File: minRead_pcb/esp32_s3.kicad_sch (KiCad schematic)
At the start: 12 parts, among them SW12 SW_Push, SW6 SW_Push, U4 ESP32-S3-WROOM-1

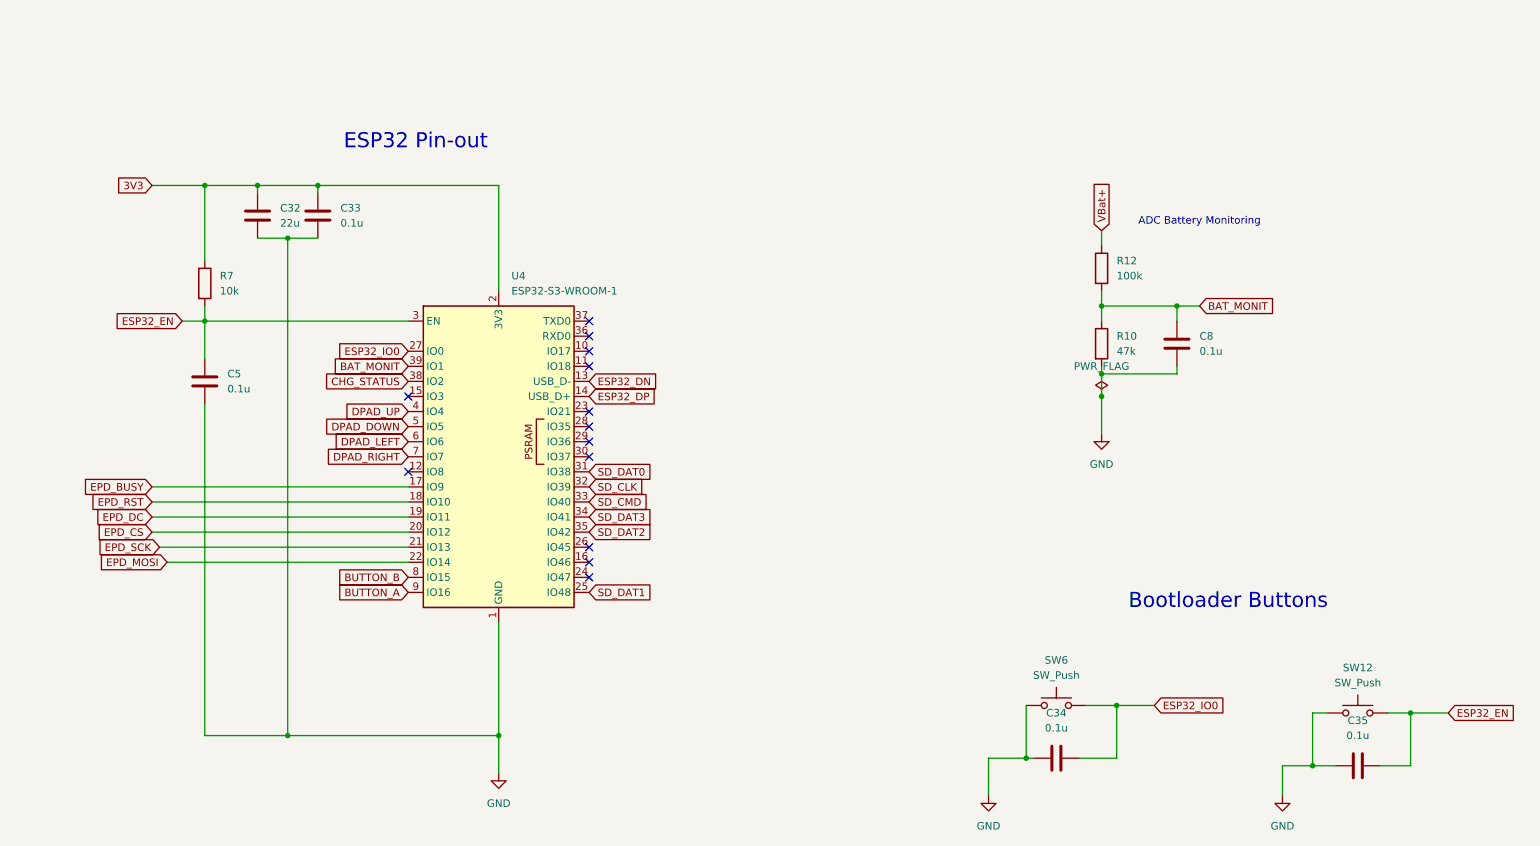
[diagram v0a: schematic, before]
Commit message: - schematic updates: - usb500 mode enabled on bq - charge limit set to 100mA 8.9kohm (safe for small batteries) - series resistors on sd card and epd lines - esd arrays for usb-c and sd-card - increased output cap for ldo from 4.7u to 22u - added pgood to gpio - confirmed reverse polarity stuff - cap to ground instead of series for sd card vdd - fixed cap values on epd
new layout:
- adjusted board size
- very compact
- need to fill ground planes and check drc errors (a lot because of solder mask)
- need to adjust jst footprint in case there's a better choice
- review review review
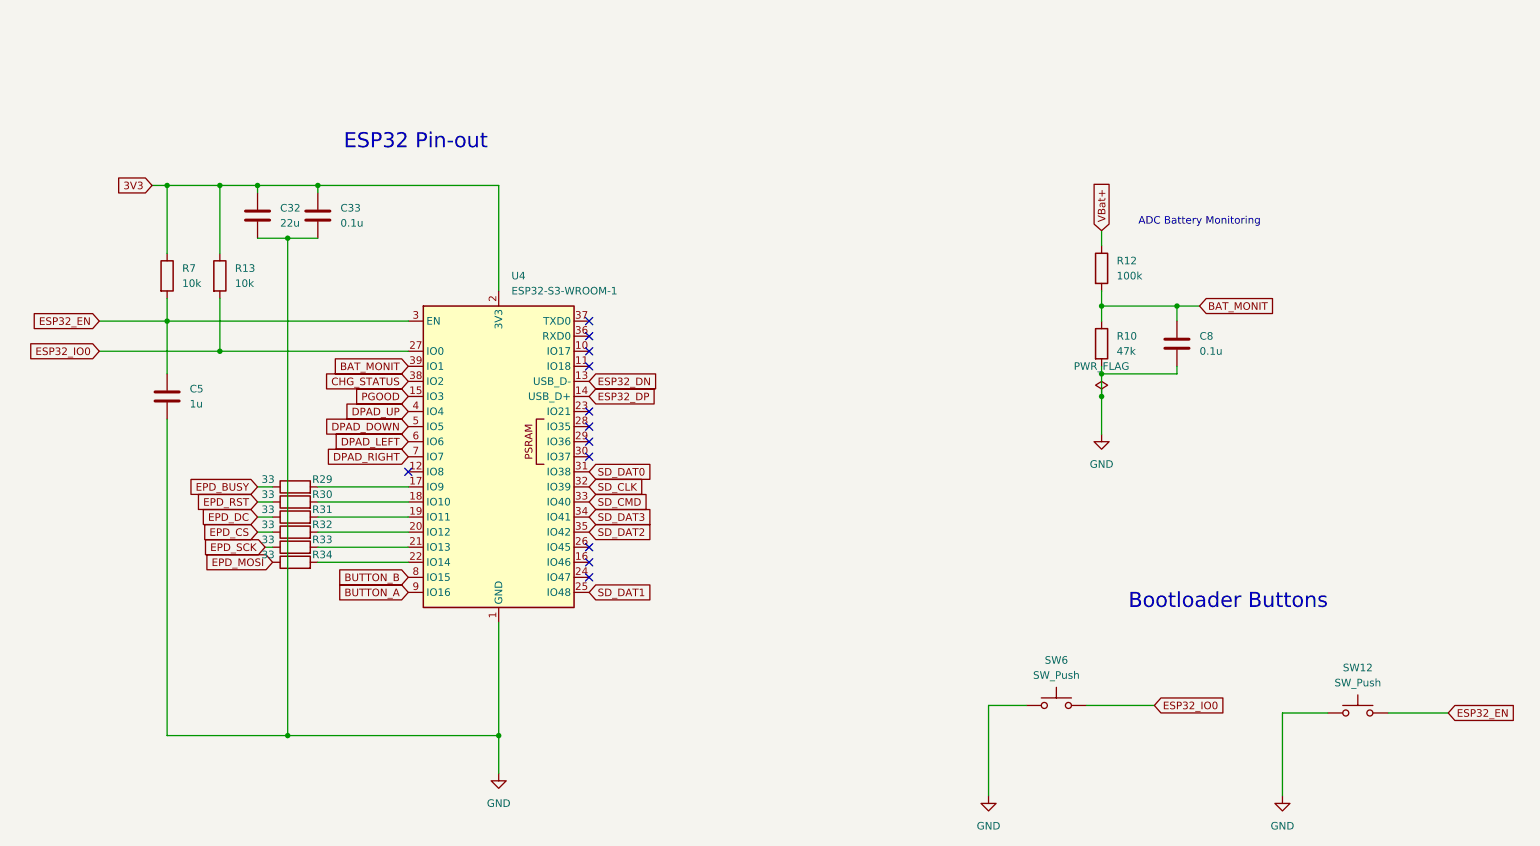
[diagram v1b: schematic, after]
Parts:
- removed C34, C35: 0.1u, Capacitor_SMD:C_0805_2012Metric_Pad1.18x1.45mm_HandSolder, symbol Device:C
- added R13: 10k, Resistor_SMD:R_0805_2012Metric_Pad1.20x1.40mm_HandSolder, symbol Device:R
- added R29, R30, R31, R32, R33, R34: 33, Resistor_SMD:R_0805_2012Metric_Pad1.20x1.40mm_HandSolder, symbol Device:R
- C5: value 0.1u -> 1u
- SW12, SW6: footprint Button_Switch_SMD:SW_SPST_TS-1088-xR020 -> Button_Switch_SMD:SW_SPST_PTS810
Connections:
- net 3V3: now also R13.1
- net EPD_BUSY: now also R29.1; no longer U4.17 (IO9)
- net EPD_CS: now also R32.1; no longer U4.20 (IO12)
- net EPD_DC: now also R31.1; no longer U4.19 (IO11)
- net EPD_MOSI: now also R34.1; no longer U4.22 (IO14)
- net EPD_RST: now also R30.1; no longer U4.18 (IO10)
- net EPD_SCK: now also R33.1; no longer U4.21 (IO13)
- net ESP32_IO0: now also R13.2
- net PGOOD: now reaches U4.15 (IO3)
- new net: R29.2, U4.17 (IO9)
- new net: R33.2, U4.21 (IO13)
- new net: R32.2, U4.20 (IO12)
- new net: R34.2, U4.22 (IO14)
- new net: R30.2, U4.18 (IO10)
- new net: R31.2, U4.19 (IO11)
- no-connect marks 13 -> 12
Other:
- moved on the sheet: C5, R7

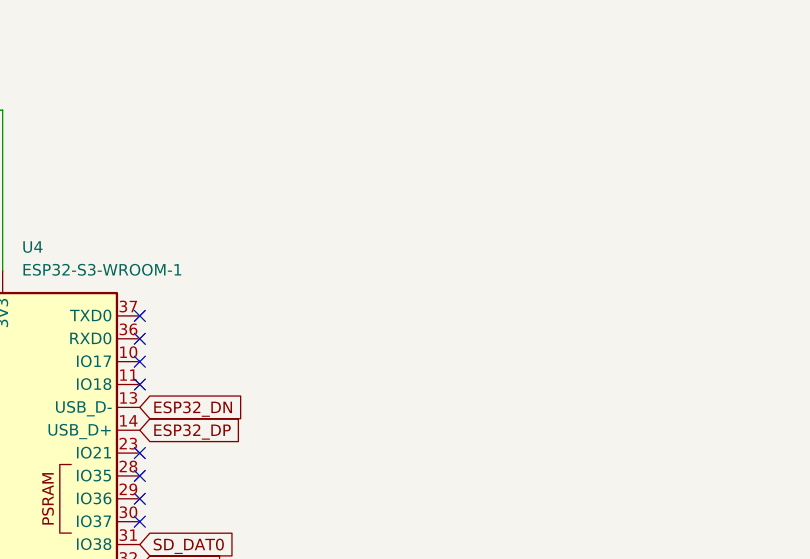
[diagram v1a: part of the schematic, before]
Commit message: draft new rev compact as possible confirmed reverse polarity circuit but need to double check jst connector made sure buttons were as evenly spaced as possible need to ensure every cap is 25v tolerant just as a default all resistors and caps are 0805 maybe double check inductor to see if we can find a better one all decoupling caps are local to their respective component updated 3d models
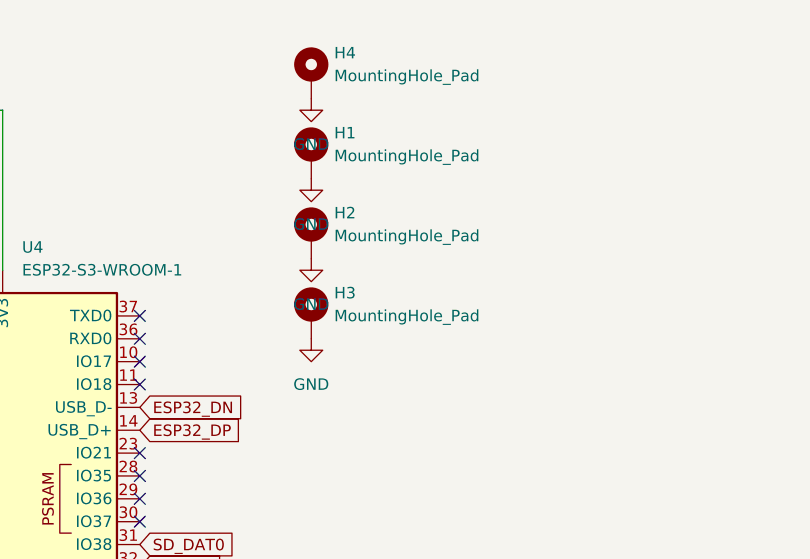
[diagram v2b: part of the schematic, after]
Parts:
- added H1, H2, H3, H4: MountingHole_Pad, MountingHole:MountingHole_2.2mm_M2_DIN965_Pad_TopBottom, symbol Mechanical:MountingHole_Pad
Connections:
- net GND: now also H1.1, H2.1, H3.1, H4.1

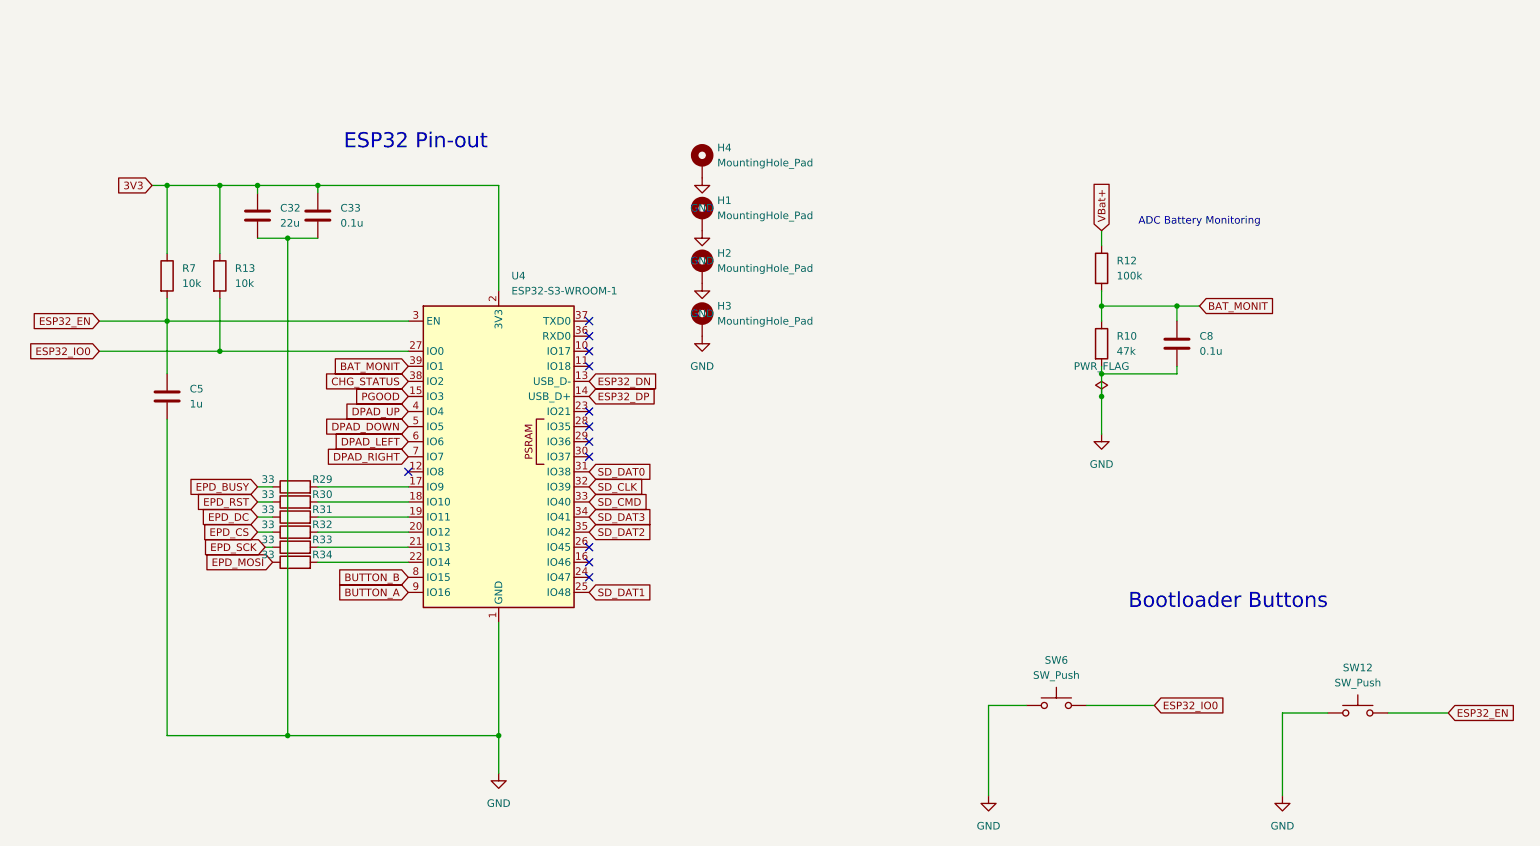
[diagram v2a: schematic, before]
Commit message: - fixed diode orientation of eink booster - everything works except eink driver: - rst pin pulls high, dc doesn't toggle, etc etc. - TODO for next rev: - remove reset stabilizer and just route 3v3 to epd inductor circuit - replace esd arrays with hand-solderable components (qfn to sot) - replace buttons with resistor ladder circuit (xteink-like) - replace bq24074 with more discrete charging circuit to aid hand-solder - add led driver (15v to 7 series LEDs) - replace usb-c receptacle with through-hole - add external dupont pins for external LED driver access and spare GPIOs
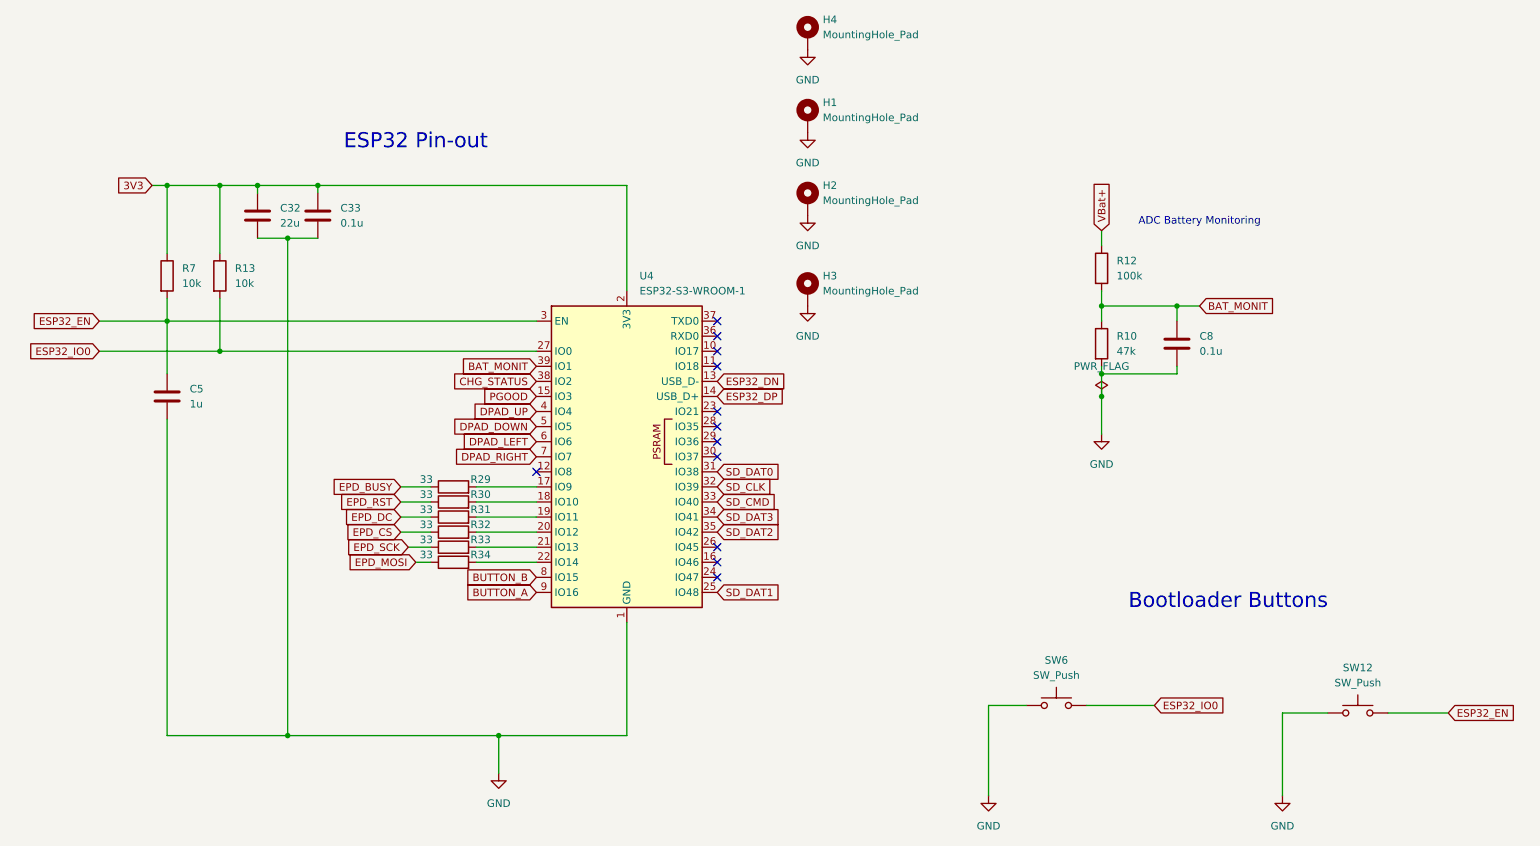
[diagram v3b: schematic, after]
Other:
- moved on the sheet: H1, H2, H3, H4, R29, R30, R31, R32, R33, R34, U4

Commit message: gigantic commit, my bad revised schematic to sanity check turns out my fpc was flipped, now fixed added following schematics: - battery protection circuit - series LED driver - external peripheral connector for unused GPIO revised following schematics: - power path, replaced with mcp charger and FET rather than bq - buttons, opted for resistor ladder circuit, added two more for xte compatibility - eink driver, opted to change to updated components from waveshare 2.3 - updated esd components for usb-c and sdmmc - updated usb-c receptacle, now through-hole
New layout:
- mostly same as last time, but work done to ensure good grounding for LED/eink circuits
- eink gpio has minimal crossing/coupling just in case
- esp32 and 24 pin headers have longer pads hopefully for easier soldering
- external header in corner back of device
- prettier passive component layout
- fat 3v3 traces and small zone fill

- todo:
- DRC errors, mostly clearance and silkscreen overlap
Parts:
- removed C32: 22u, Capacitor_SMD:C_0805_2012Metric_Pad1.18x1.45mm_HandSolder, symbol Device:C
- removed C33, C8: 0.1u, Capacitor_SMD:C_0805_2012Metric_Pad1.18x1.45mm_HandSolder, symbol Device:C
- removed C5: 1u, Capacitor_SMD:C_0805_2012Metric_Pad1.18x1.45mm_HandSolder, symbol Device:C
- removed H1, H2, H3, H4: MountingHole_Pad, MountingHole:MountingHole_2.2mm_M2_DIN965_Pad_TopBottom, symbol Mechanical:MountingHole_Pad
- removed R10: 47k, Resistor_SMD:R_0805_2012Metric_Pad1.20x1.40mm_HandSolder, symbol Device:R
- removed R12: 100k, Resistor_SMD:R_0805_2012Metric_Pad1.20x1.40mm_HandSolder, symbol Device:R
- removed R13, R7: 10k, Resistor_SMD:R_0805_2012Metric_Pad1.20x1.40mm_HandSolder, symbol Device:R
- removed R29, R30, R31, R32, R33, R34: 33, Resistor_SMD:R_0805_2012Metric_Pad1.20x1.40mm_HandSolder, symbol Device:R
- removed SW12, SW6: SW_Push, Button_Switch_SMD:SW_SPST_PTS810, symbol Switch:SW_Push
- removed U4: ESP32-S3-WROOM-1, RF_Module:ESP32-S3-WROOM-1, symbol RF_Module:ESP32-S3-WROOM-1
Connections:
- no-connect marks 12 -> 0
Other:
- note removed: "ADC Battery Monitoring"
- note removed: "Bootloader Buttons"
- note removed: "ESP32 Pin-out"
